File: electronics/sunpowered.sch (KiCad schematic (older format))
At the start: 11 parts

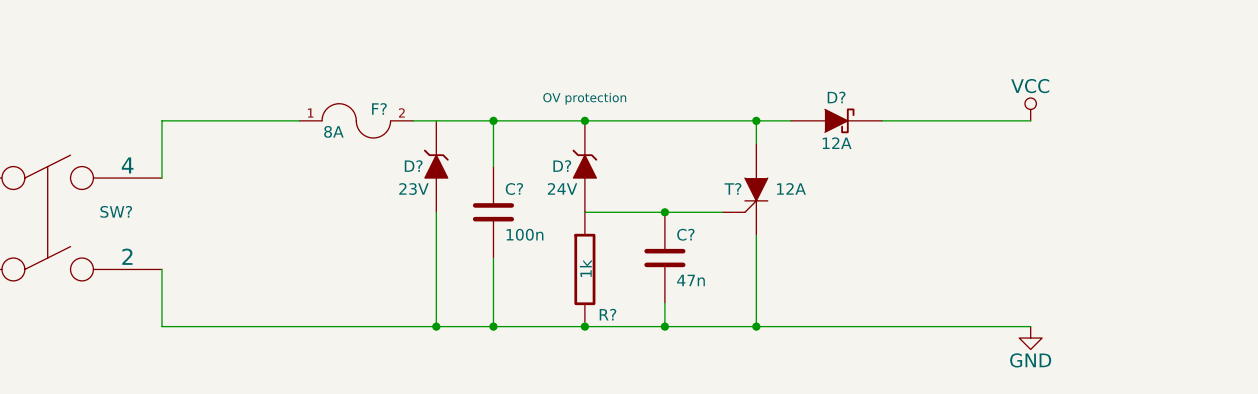
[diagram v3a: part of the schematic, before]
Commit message: mosfet switch at the end of the input stage
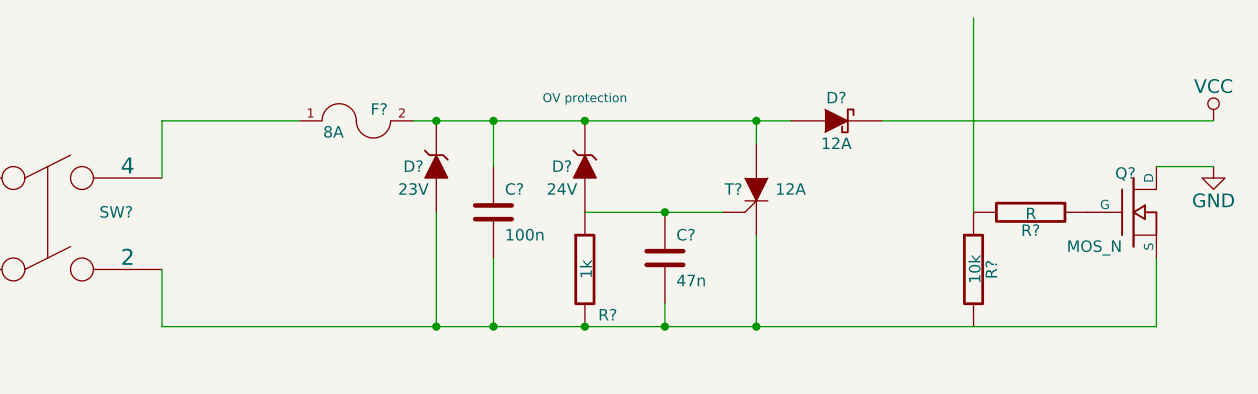
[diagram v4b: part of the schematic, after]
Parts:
- added Q?: MOS_N, symbol MOS_N
- added R?: 10k, symbol R
- added R?: R, symbol R
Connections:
- wire segments 13 -> 16
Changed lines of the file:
@@
 $EndComp
 Wire Wire Line
-	4300 2050 4300 2150
+	4300 2150 4300 2050
 Connection ~ 4300 2150
 $Comp
@@
 Connection ~ 4700 1250
 Wire Wire Line
-	4700 1750 4700 2150
+	4700 2150 4700 1750
 Connection ~ 4700 2150
 Connection ~ 4300 1650
@@
 Wire Wire Line
 	3200 1250 4850 1250
-$Comp
-L GND #PWR?
-U 1 1 54D5467F
-P 5900 2150
-F 0 "#PWR?" H 5900 1900 60  0001 C CNN
-F 1 "GND" H 5900 2000 60  0000 C CNN
-F 2 "" H 5900 2150 60  0000 C CNN
-F 3 "" H 5900 2150 60  0000 C CNN
-	1    5900 2150
-	1    0    0    -1
-$EndComp
-$Comp
-L VCC #PWR?
-U 1 1 54D547B5
-P 5900 1250
-F 0 "#PWR?" H 5900 1100 60  0001 C CNN
-F 1 "VCC" H 5900 1400 60  0000 C CNN
-F 2 "" H 5900 1250 60  0000 C CNN
-F 3 "" H 5900 1250 60  0000 C CNN
-	1    5900 1250
-	1    0    0    -1
-$EndComp
 $Comp
 L DPST SW?
@@
 	3550 1450 3550 1250
 Connection ~ 3550 1250
-Wire Wire Line
-	5250 1250 5900 1250
 $Comp
 L ZENER D?
@@
 	2100 1900 2100 2150
 Wire Wire Line
-	2100 2150 5900 2150
+	5250 1250 6700 1250
+Wire Wire Line
+	2100 2150 6450 2150
+$Comp
+L MOS_N Q?
+U 1 1 54D70F3D
+P 6350 1650
+F 0 "Q?" H 6360 1820 50  0000 R CNN
+F 1 "MOS_N" H 6300 1500 50  0000 R CNN
+F 2 "" H 6350 1650 60  0000 C CNN
+F 3 "" H 6350 1650 60  0000 C CNN
+	1    6350 1650
+	1    0    0    -1
+$EndComp
+Wire Wire Line
+	6450 2150 6450 1850
+$Comp
+L R R?
+U 1 1 54D70FF3
+P 5650 1900
+F 0 "R?" V 5730 1900 50  0000 C CNN
+F 1 "10k" V 5657 1901 50  0000 C CNN
+F 2 "" V 5580 1900 30  0000 C CNN
+F 3 "" H 5650 1900 30  0000 C CNN
+	1    5650 1900
+	1    0    0    -1
+$EndComp
+Connection ~ 3300 1250
+Wire Wire Line
+	6450 1450 6700 1450
+$Comp
+L GND #PWR?
+U 1 1 54D712EB
+P 6700 1450
+F 0 "#PWR?" H 6700 1200 60  0001 C CNN
+F 1 "GND" H 6700 1300 60  0000 C CNN
+F 2 "" H 6700 1450 60  0000 C CNN
+F 3 "" H 6700 1450 60  0000 C CNN
+	1    6700 1450
+	1    0    0    -1
+$EndComp
+$Comp
+L VCC #PWR?
+U 1 1 54D7132A
+P 6700 1250
+F 0 "#PWR?" H 6700 1100 60  0001 C CNN
+F 1 "VCC" H 6700 1400 60  0000 C CNN
+F 2 "" H 6700 1250 60  0000 C CNN
+F 3 "" H 6700 1250 60  0000 C CNN
+	1    6700 1250
+	1    0    0    -1
+$EndComp
+$Comp
+L R R?
+U 1 1 54D7146D
+P 5900 1650
+F 0 "R?" V 5980 1650 50  0000 C CNN
+F 1 "R" V 5907 1651 50  0000 C CNN
+F 2 "" V 5830 1650 30  0000 C CNN
+F 3 "" H 5900 1650 30  0000 C CNN
+	1    5900 1650
+	0    1    1    0
+$EndComp
+Wire Wire Line
+	5650 1650 5650 800
 $EndSCHEMATC

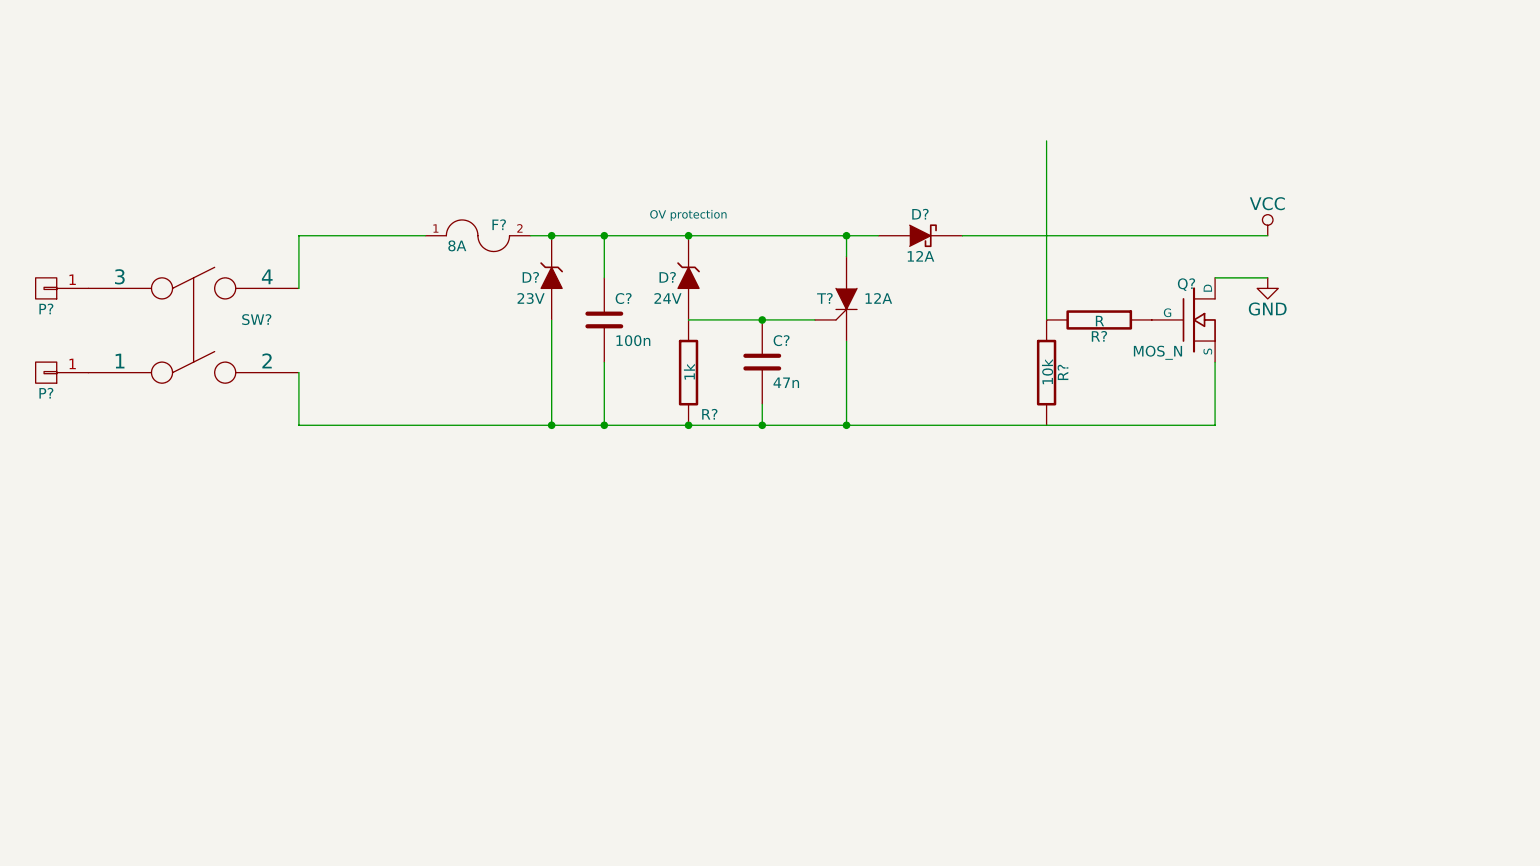
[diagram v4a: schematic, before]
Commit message: current sensor added on the front
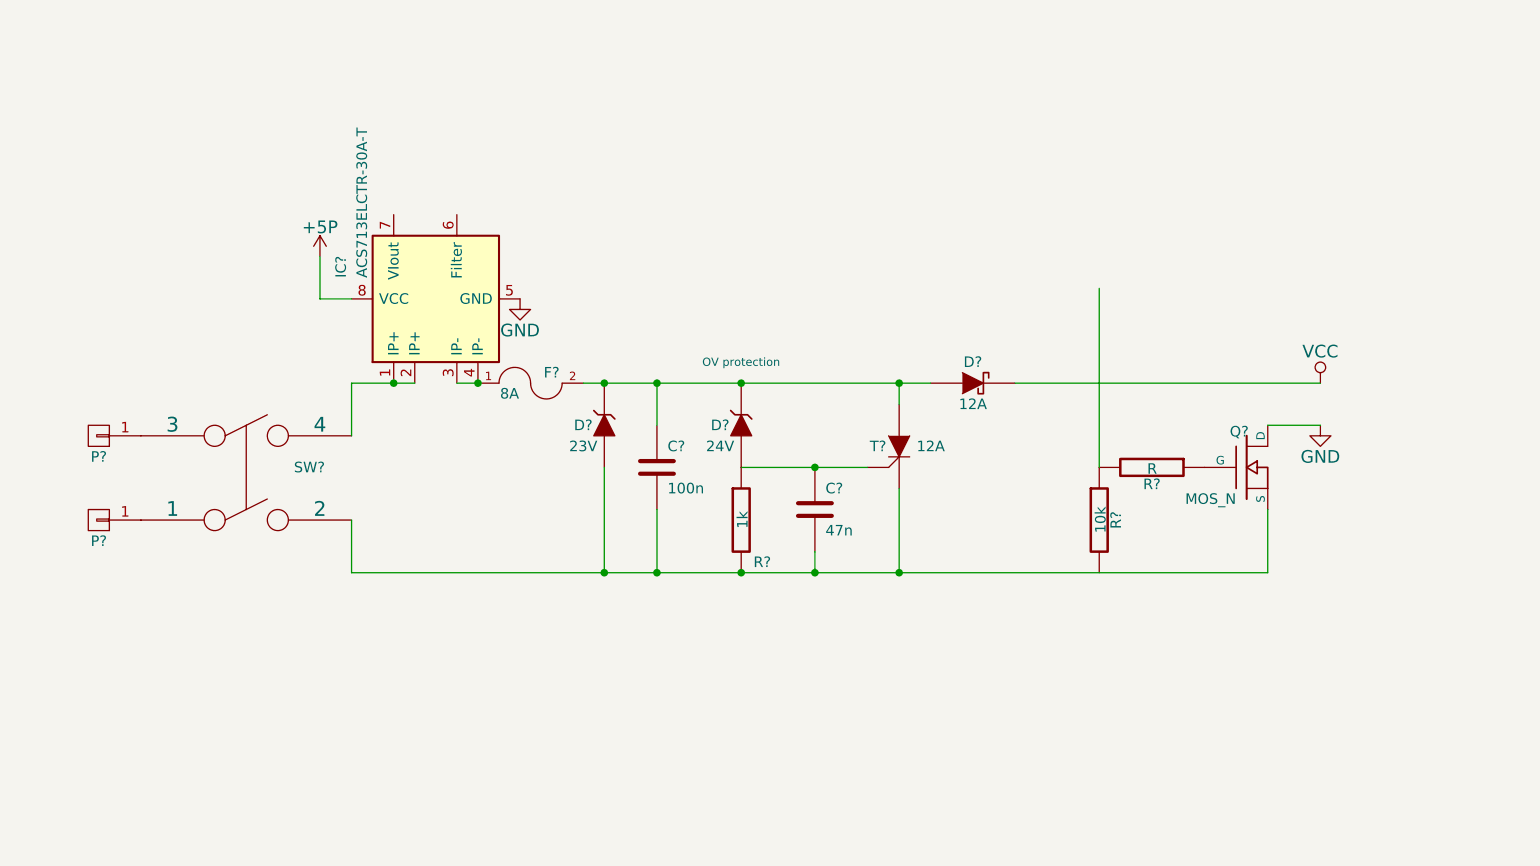
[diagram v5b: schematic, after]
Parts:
- added IC?: ACS713ELCTR-30A-T, Housings_SOIC:SOIC-8_3.9x4.9mm_Pitch1.27mm, symbol ACS713ELCTR-30A-T
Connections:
- net labels added: +5P
- wire segments 16 -> 19
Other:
- moved on the sheet: C?, D?, F?, P?, Q?, R?, SW?, T?

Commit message: current sensor placement corrected
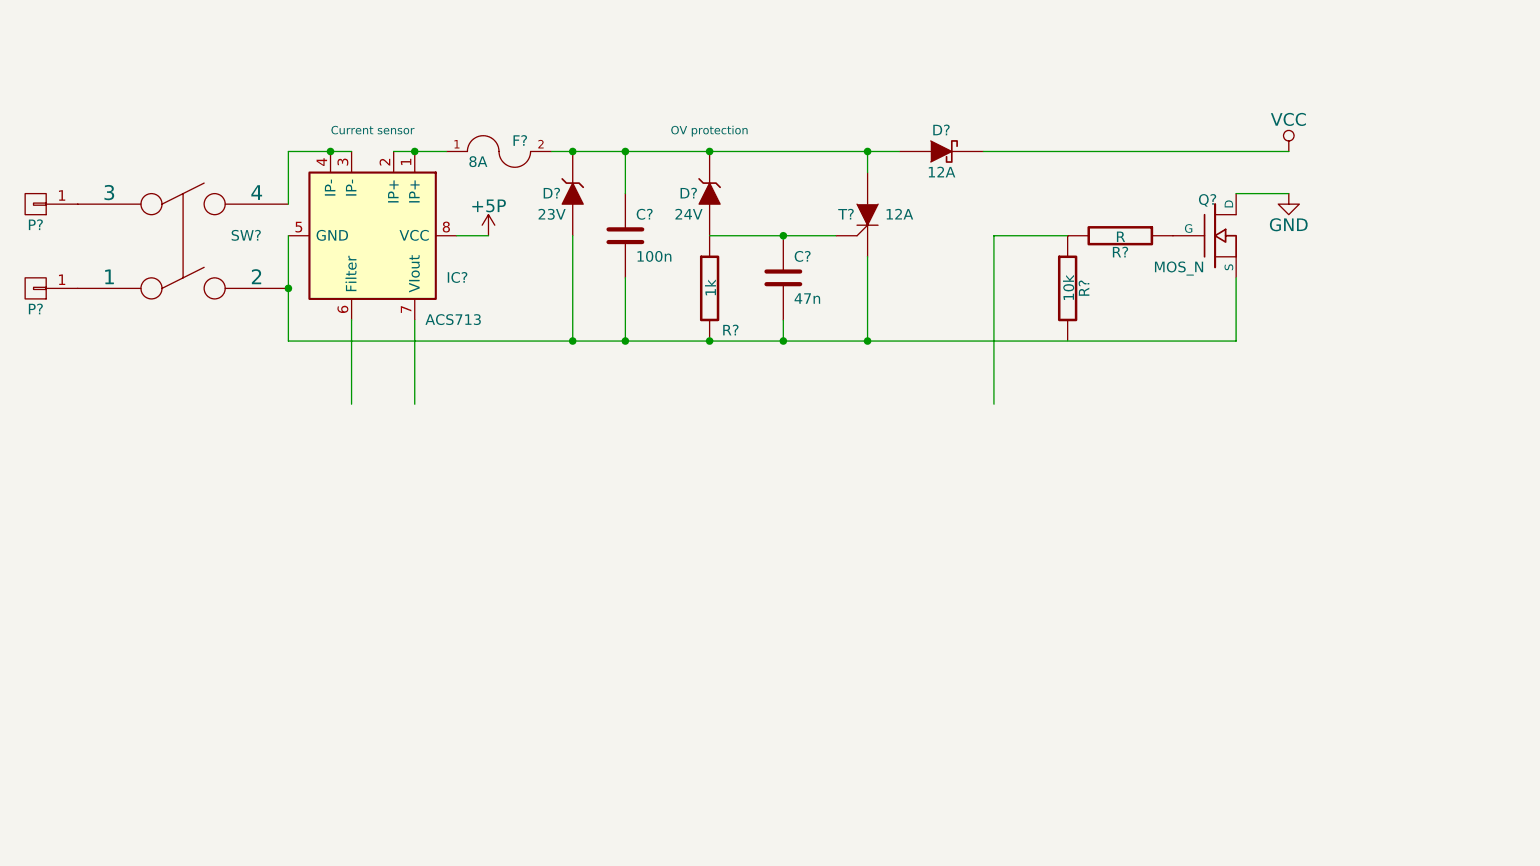
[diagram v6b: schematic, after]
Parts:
- IC?: value ACS713ELCTR-30A-T -> ACS713; Note (none) -> Current sensor
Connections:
- wire segments 19 -> 21
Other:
- moved on the sheet: C?, D?, F?, IC?, P?, Q?, R?, SW?, T?

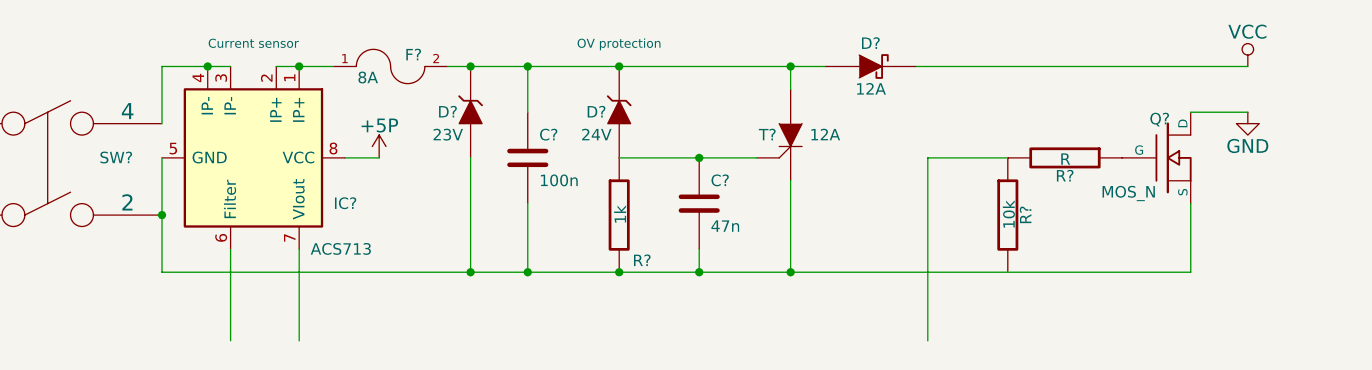
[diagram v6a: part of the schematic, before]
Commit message: fuse before current sensor
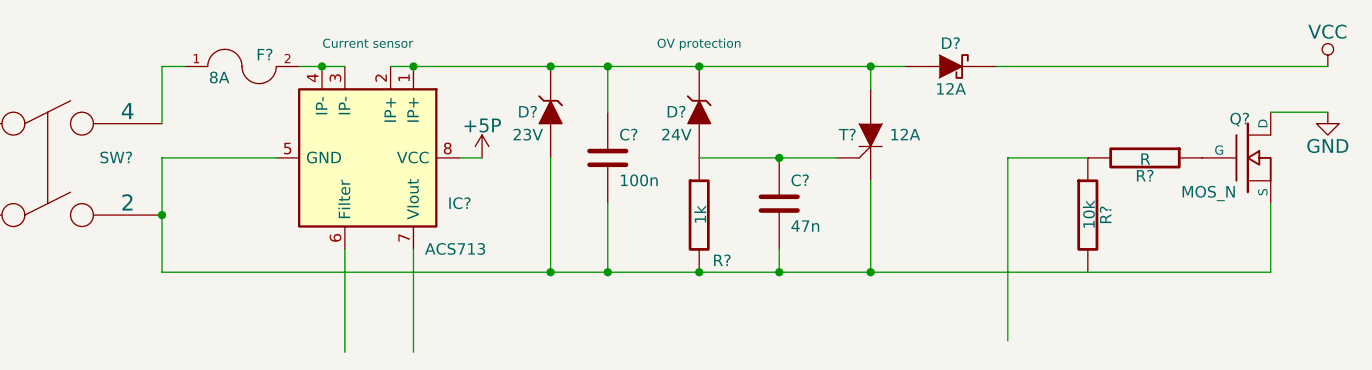
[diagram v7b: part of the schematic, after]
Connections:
- wire segments 21 -> 22
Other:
- moved on the sheet: C?, D?, F?, IC?, Q?, R?, T?

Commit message: minor wires cleanup
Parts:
- added C?: 0.1uF, symbol C
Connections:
- wire segments 22 -> 45
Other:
- moved on the sheet: C?, D?, F?, IC?, P?, Q?, R?, SW?, T?
